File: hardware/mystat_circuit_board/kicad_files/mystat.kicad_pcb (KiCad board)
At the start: 4 copper layers, 60 x 81 mm, 93 parts, among them J1 PJ-063AH, J2 2173157-3, J3 SJ1-42534-SMT, K1 9011-05-11, K2 9011-05-11, K3 9011-05-11, K4 9011-05-11, K5 9011-05-11, P1 ICSP, U10 OPA192, U11 BUF634A, U12 ADG1419, U13 OPA192, U14 OPA192, U15 OPA192, U16 OPA192, U17 OPA192, U2 LTM8045, U3 ADP7182AUJZ-R7, U4 ADP7118AUJZ-5.0-R7, U5 PIC16F1459, U6 ADR421, U7 MCP3550-60, U8 MCP3550-60, U9 DAC1220, X1 2.5 MHz

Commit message: schematic: change electrode connections to screw terminals, BUF634A to HSOIC version with thermal pad
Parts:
- C10, C11, C12, C13, C14, C15, C17, C18, C2, C23, C25, C26, C27, C28, C29, C30, C31, C32, C34, C35, C36, C37: value 0.1 µF -> 100 nF
- C16: value 10 µF -> 10 uF
- C3: value 47 μF -> 47 uF
- C39, C5, C6, C8, C9: value 4.7 µF -> 4.7 uF
- C4, C7: value 4.7 μF -> 4.7 uF
- FB1: value Ferrite_Bead -> 32 Ω
- U11: value BUF634A -> BUF634AIDDAR; footprint my_footprints:SOIC-8 -> Package_SO:TI_SO-PowerPAD-8_ThermalVias
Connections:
- J2 pad 4: (no net) -> unconnected-(J2-Pad4)
- P1 pad 6: (no net) -> unconnected-(P1-Pin_6-Pad6)
- U11 pad 1: (no net) -> unconnected-(U11-BW-Pad1)
- U11 pad 2: (no net) -> unconnected-(U11-NC-Pad2)
- U11 pad 5: (no net) -> unconnected-(U11-NC-Pad5)
- U11 pad 8: (no net) -> unconnected-(U11-NC-Pad8)
- U12 pad 5: (no net) -> unconnected-(U12-NC-Pad5)
- U2 pad E1: (no net) -> unconnected-(U2-PIN_E1-PadE1)
- U2 pad F1: (no net) -> unconnected-(U2-PIN_F1-PadF1)
- U5 pad 14: (no net) -> unconnected-(U5-RC2-Pad14)
- U6 pad 1: (no net) -> unconnected-(U6-TP-Pad1)
- U6 pad 3: (no net) -> unconnected-(U6-NIC-Pad3)
- U6 pad 5: (no net) -> unconnected-(U6-TRIM-Pad5)
- U6 pad 7: (no net) -> unconnected-(U6-NIC-Pad7)
- U6 pad 8: (no net) -> unconnected-(U6-TP-Pad8)
- U9 pad 6: (no net) -> unconnected-(U9-DNC-Pad6)
- U9 pad 7: (no net) -> unconnected-(U9-DNC-Pad7)
- U9 pad 8: (no net) -> unconnected-(U9-DNC-Pad8)
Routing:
- net Net-(U10-~): track 11.5 -> 0.00 mm
- net (no net): track 0.00 -> 11.5 mm
- net GND: vias 55 -> 54
- added copper zone on B.Cu, net -13.4V

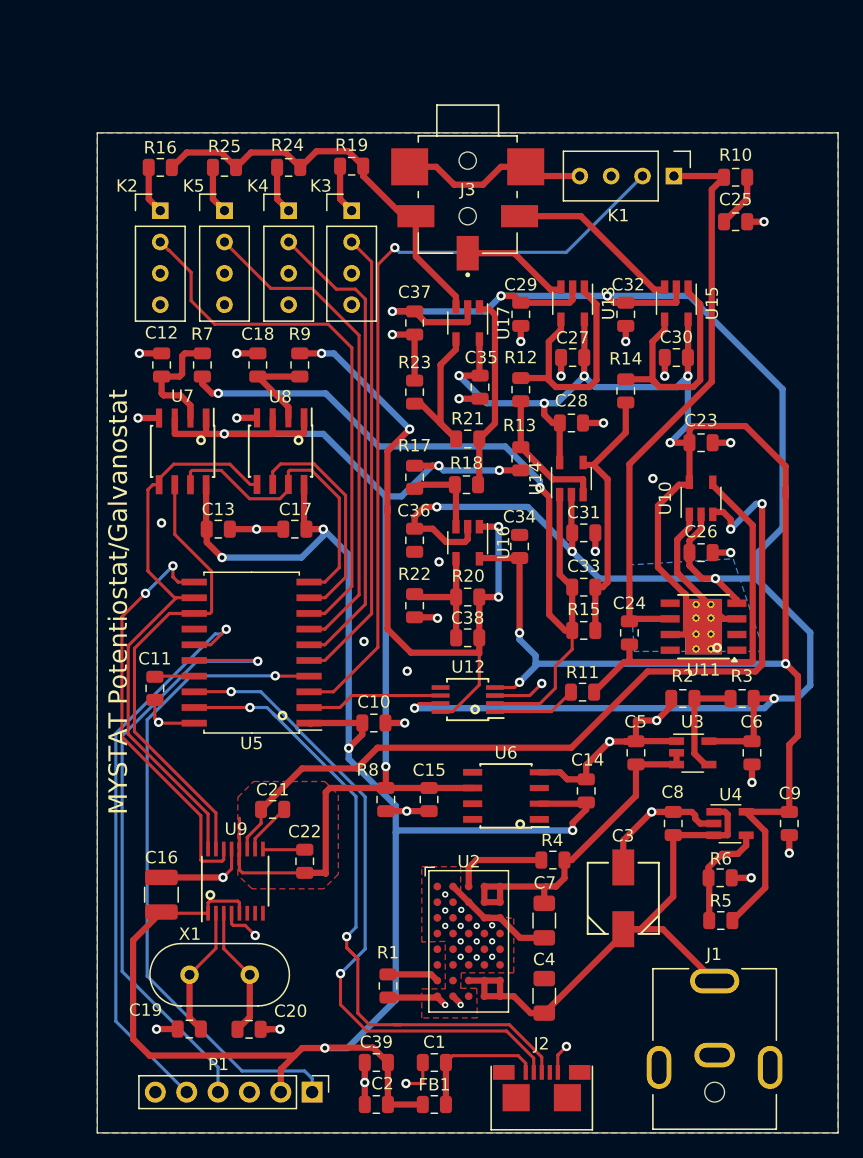
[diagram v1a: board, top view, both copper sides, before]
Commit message: change micro USB to USB C 16P 2.0, rotate U11 for routing of thermal pad version
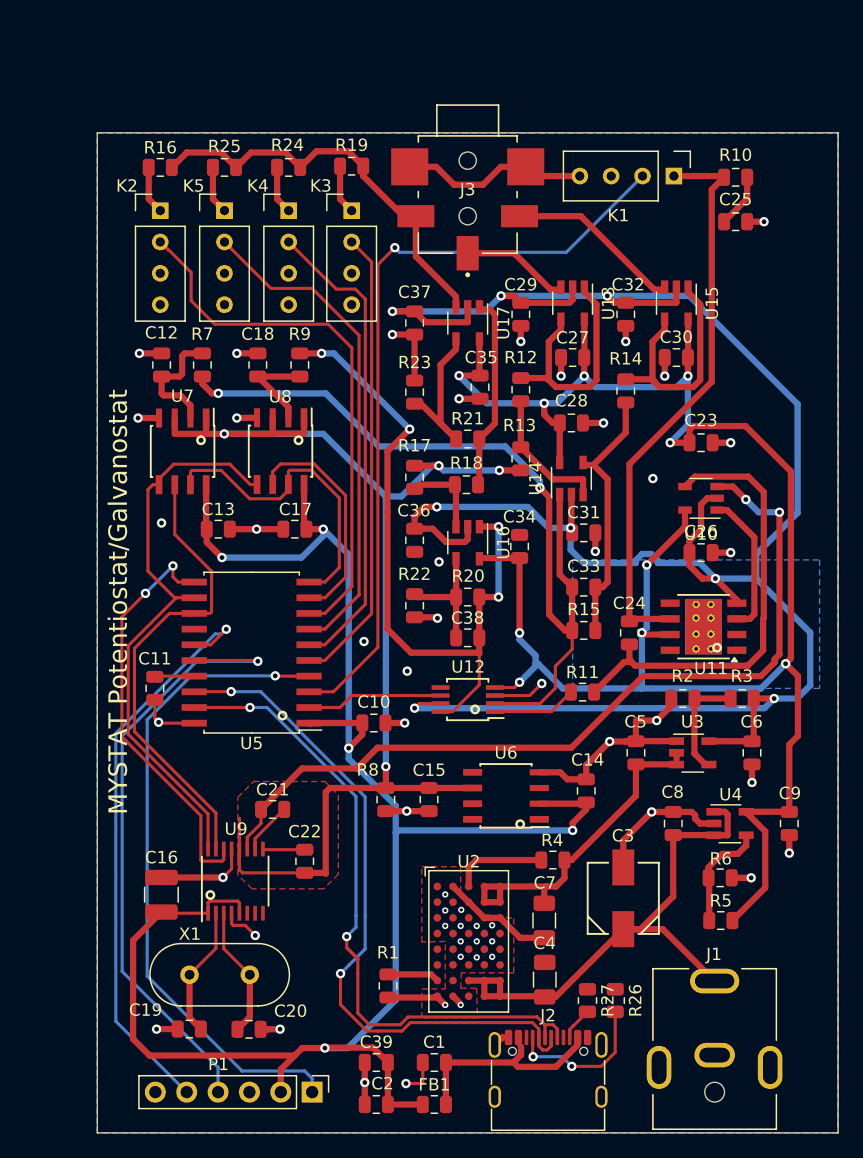
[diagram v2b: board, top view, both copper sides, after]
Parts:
- added R26: 5.1k, Resistor_SMD:R_0805_2012Metric, F.Cu at (92.0, 120.3)
- added R27: 5.1k, Resistor_SMD:R_0805_2012Metric, F.Cu at (89.7, 120.3)
- J2: value 2173157-3 -> ~; footprint my_footprints:CONN_2173157-3 -> my_footprints:USB_C_Receptacle_G-Switch_GT-USB-7010ASV
- U7, U8: value MCP3550-60 -> MCP3551
- moved C4 1.31 mm to (86.2, 118.6)
- moved J2 1.03 mm to (86.5, 127.0)
- turned U10 to 180 degrees
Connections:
- J2 pad 1: Net-(C1-Pad2) -> GND
- J2 pad 2: Net-(U5-D-) -> GND
- J2 pad 3: Net-(U5-D+) -> GND
- J2 pad 4: unconnected-(J2-Pad4) -> GND
- U5 pad 18: Net-(U5-D-) -> /digital/D-
- U5 pad 19: Net-(U5-D+) -> /digital/D+
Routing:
- net /digital/D-: track 0.00 -> 55.4 mm, vias 0 -> 2
- net /digital/D+: track 0.00 -> 54.4 mm, vias 0 -> 2
- net Net-(U5-D+): track 54.0 -> 0.00 mm, vias 2 -> 0
- net Net-(U5-D-): track 53.2 -> 0.00 mm, vias 2 -> 0
- net Net-(J2-CC1): track 0.00 -> 12.3 mm, vias 0 -> 2
- net Net-(U10-~): track 0.00 -> 11.7 mm
- net (no net): track 11.5 -> 0.00 mm
- net Net-(C1-Pad2): track 11.1 -> 19.2 mm
- net GND: track 635.0 -> 641.2 mm, vias 54 -> 53
- net Net-(U10--): track 31.2 -> 36.9 mm
- net -13.4V: track 179.2 -> 184.8 mm
- net Net-(J2-CC2): track 0.00 -> 2.68 mm
- net +15V: track 46.5 -> 45.2 mm
- net +13.4V: track 159.4 -> 159.6 mm, vias 8 -> 10
- added copper zone on In1.Cu, net -13.4V
- added copper zone on In2.Cu, net -13.4V

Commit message: partway through adding normal reed relay size
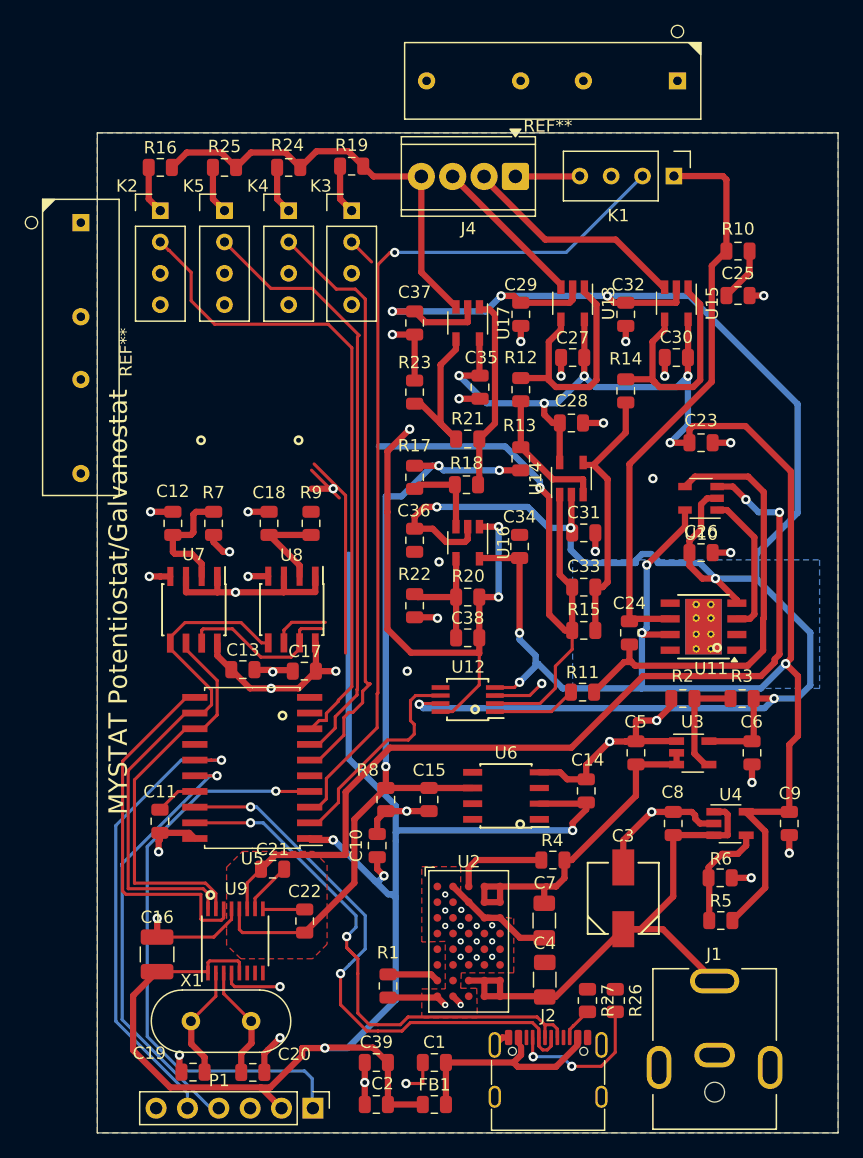
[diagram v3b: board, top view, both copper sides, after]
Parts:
- removed J3: SJ1-42534-SMT, my_footprints:CUI_SJ1-42534-SMT
- added J4: Screw_Terminal_01x04, TerminalBlock_Phoenix:TerminalBlock_Phoenix_MPT-0,5-4-2.54_1x04_P2.54mm_Horizontal, F.Cu at (83.9, 53.5)
- added REF**: Reed_Relay_MiRelay_SIP-HV1A05D, my_footprints:Reed_Relay_MiRelay_SIP-HV1A05D, F.Cu at (48.7, 57.3)
- added REF**: Reed_Relay_MiRelay_SIP-HV1A05D, my_footprints:Reed_Relay_MiRelay_SIP-HV1A05D, F.Cu at (97.0, 45.8)
- moved C12 12.9 mm to (56.1, 81.6)
- moved C18 12.9 mm to (63.9, 81.6)
- moved R7 12.9 mm to (59.4, 81.6)
- moved R9 12.9 mm to (67.3, 81.6)
- moved U7 12.9 mm to (57.8, 88.6)
- moved U8 12.9 mm to (65.7, 88.6)
- moved C13 11.6 mm to (61.8, 93.5)
- moved C17 11.5 mm to (66.8, 93.6)
- moved C11 10.8 mm to (55.1, 105.8)
- moved C10 9.93 mm to (72.7, 107.7), turned to 90 degrees
- moved U5 9.34 mm to (62.5, 101.4)
- moved C25 5.98 mm to (101.9, 63.2)
- moved R10 5.98 mm to (101.9, 59.6)
- moved C16 4.84 mm to (54.8, 116.5)
- moved C21 4.84 mm to (64.2, 109.6)
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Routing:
- net RANGE3: track 37.4 -> 2.29 mm
- net Vref: track 98.4 -> 82.2 mm
- net V_MEAS: track 67.0 -> 52.2 mm
- net Net-(P1-Pin_4): track 50.8 -> 36.1 mm
- net SDIO2: track 18.5 -> 4.65 mm
- net GND: track 641.2 -> 629.1 mm, vias 53 -> 50
- net CS2: track 25.4 -> 13.7 mm
- net WE: track 15.3 -> 5.23 mm
- net I_MEAS: track 56.8 -> 66.7 mm
- net RANGE2: track 38.7 -> 48.4 mm
- net /digital/D-: track 55.4 -> 45.8 mm
- net /digital/D+: track 54.4 -> 44.8 mm
- net RANGE1: track 40.2 -> 49.3 mm
- net RANGE4: track 44.1 -> 53.1 mm
- net Net-(P1-Pin_5): track 47.0 -> 38.2 mm
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
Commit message: progress save with layout
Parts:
- removed REF** (x2): Reed_Relay_MiRelay_SIP-HV1A05D, my_footprints:Reed_Relay_MiRelay_SIP-HV1A05D
- removed REF**: LOGO, my_footprints:GPLv3_2
- removed REF**: OSHW-Logo2_14.6x12mm_SilkScreen, Symbol:OSHW-Logo2_14.6x12mm_SilkScreen
- K1, K2, K3, K4, K5: value 9011-05-11 -> ~; footprint my_footprints:relay_9011-05-11 -> my_footprints:Reed_Relay_MiRelay_SIP-HV1A05D
- moved K3 21.6 mm to (77.3, 76.8), turned to 90 degrees
- moved K4 21.1 mm to (70.3, 76.8), turned to 90 degrees
- moved K5 20.7 mm to (63.2, 76.8), turned to 90 degrees
- moved K2 20.6 mm to (56.1, 76.8), turned to 90 degrees
- moved R10 13.6 mm to (99.3, 73.0), turned to -90 degrees
- moved C25 11.7 mm to (96.8, 73.7), turned to 90 degrees
- moved C37 11.6 mm to (81.9, 55.6), turned to 90 degrees
- moved J4 11.4 mm to (95.2, 53.8)
- moved R23 10.3 mm to (82.9, 63.7), turned to 180 degrees
- moved K1 7.41 mm to (104.1, 53.3)
- moved R19 7.32 mm to (77.9, 52.7)
- moved U17 6.97 mm to (83.7, 59.5)
- moved R21 5.96 mm to (85.2, 71.9)
- moved C23 5.66 mm to (104.1, 77.4)
- moved C28 5.52 mm to (92.5, 69.8)
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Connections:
- K1 pad 1: Net-(C24-Pad1) -> WE
- K1 pad 2: CELL_ON -> GND
- K1 pad 3: GND -> CELL_ON
- K1 pad 4: WE -> Net-(C24-Pad1)
- K2 pad 1: Net-(K2-~-Pad1) -> GND
- K2 pad 2: RANGE4 -> GND
- K2 pad 3: GND -> RANGE4
- K2 pad 4: GND -> Net-(K2-Pad4)
- K3 pad 1: Net-(K3-~-Pad1) -> GND
- K3 pad 2: RANGE3 -> GND
- K3 pad 3: GND -> RANGE3
- K3 pad 4: GND -> Net-(K3-Pad4)
- K4 pad 1: Net-(K4-~-Pad1) -> GND
- K4 pad 2: RANGE2 -> GND
- K4 pad 3: GND -> RANGE2
- K4 pad 4: GND -> Net-(K4-Pad4)
- K5 pad 1: Net-(K5-~-Pad1) -> GND
- K5 pad 2: RANGE1 -> GND
- K5 pad 3: GND -> RANGE1
- K5 pad 4: GND -> Net-(K5-Pad4)
- R16 pad 2: Net-(K2-~-Pad1) -> Net-(K2-Pad4)
- R19 pad 2: Net-(K3-~-Pad1) -> Net-(K3-Pad4)
- R24 pad 2: Net-(K4-~-Pad1) -> Net-(K4-Pad4)
- R25 pad 2: Net-(K5-~-Pad1) -> Net-(K5-Pad4)
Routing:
- net RANGE3: track 2.29 -> 41.7 mm
- net GND: track 629.1 -> 653.1 mm, vias 50 -> 55
- net I_MEAS: track 66.7 -> 44.4 mm
- net Net-(C24-Pad1): track 46.8 -> 29.7 mm
- net Net-(U10--): track 36.9 -> 21.7 mm, vias 0 -> 2
- net V_MEAS: track 52.2 -> 67.2 mm
- net Vref: track 82.2 -> 96.1 mm
- net RE: track 18.4 -> 5.97 mm
- net +5V: track 140.7 -> 128.3 mm, vias 6 -> 5
- net Net-(U17-~): track 15.8 -> 26.0 mm
- net Net-(U15--): track 20.0 -> 29.7 mm
- net SDIO2: track 4.65 -> 12.8 mm
- net RANGE2: track 48.4 -> 40.3 mm
- net CS2: track 13.7 -> 21.0 mm
- net RANGE1: track 49.3 -> 42.2 mm
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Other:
- board text added: "Eclectic version 8"
- board text removed: "Lucky version 7"

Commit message: more pcb layout progress save
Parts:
- C3: footprint my_footprints:EEE-FT1V470AR -> easyeda2kicad:CAP-SMD_BD5.0-L5.3-W5.3-LS6.0-FD
- FB1: value 32 Ω -> 33 Ω
- J4: footprint TerminalBlock_Phoenix:TerminalBlock_Phoenix_MPT-0,5-4-2.54_1x04_P2.54mm_Horizontal -> easyeda2kicad:CONN-TH_4P-P2.54_MX128-2.54-GN01-04P-CU-Y-A
- moved J4 4.08 mm to (91.2, 53.8)
- moved C4 3.78 mm to (86.3, 114.8)
- moved C7 3.78 mm to (86.2, 110.0)
- moved U2 3.78 mm to (80.1, 111.7)
- moved R1 3.78 mm to (73.6, 115.3)
- moved C14 3.37 mm to (89.5, 99.9)
- moved U6 3.09 mm to (84.3, 100.8)
- moved R4 2.96 mm to (87.0, 105.9)
- moved C15 2.81 mm to (78.9, 101.2)
- moved R11 2.61 mm to (90.2, 92.9)
- moved R8 1.81 mm to (76.4, 102.7)
- moved R27 1.41 mm to (88.3, 120.1)
- moved R26 0.88 mm to (91.1, 120.1)
- moved C37 0.53 mm to (82.1, 55.1)
- moved C23 0.30 mm to (104.0, 77.1)
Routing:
- net GND: track 653.1 -> 619.4 mm, vias 55 -> 56
- net Net-(C1-Pad2): track 18.2 -> 28.0 mm, vias 0 -> 2
- net /digital/D-: track 49.0 -> 45.9 mm
- net Net-(U12-D): track 6.81 -> 9.41 mm
- net Net-(U10--): track 21.7 -> 19.4 mm
- net /digital/D+: track 48.1 -> 45.8 mm
- net Net-(C24-Pad1): track 29.7 -> 31.9 mm
- net -15V: track 28.2 -> 26.0 mm
- net Vref: track 96.1 -> 98.1 mm
- net +15V: track 45.1 -> 43.5 mm
- net -13.4V: track 185.2 -> 186.8 mm
- net DAC_out: track 72.9 -> 74.4 mm
- net Net-(J2-CC1): track 12.3 -> 13.7 mm, vias 2 -> 0
- net Net-(U2-PIN_A3): track 7.66 -> 6.86 mm
- net +5V: track 128.3 -> 129.1 mm
- added copper zone on F.Cu, net -13.4V

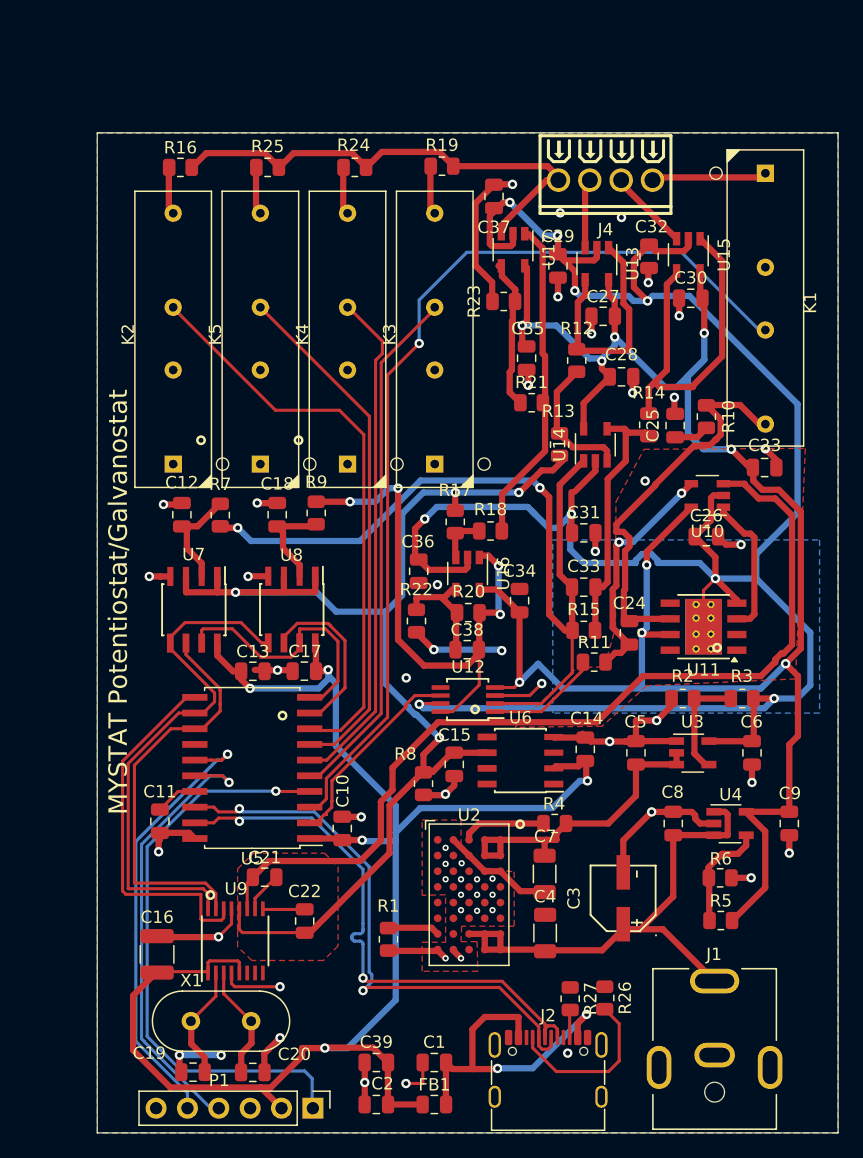
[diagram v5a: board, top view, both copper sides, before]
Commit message: silkscreen changes
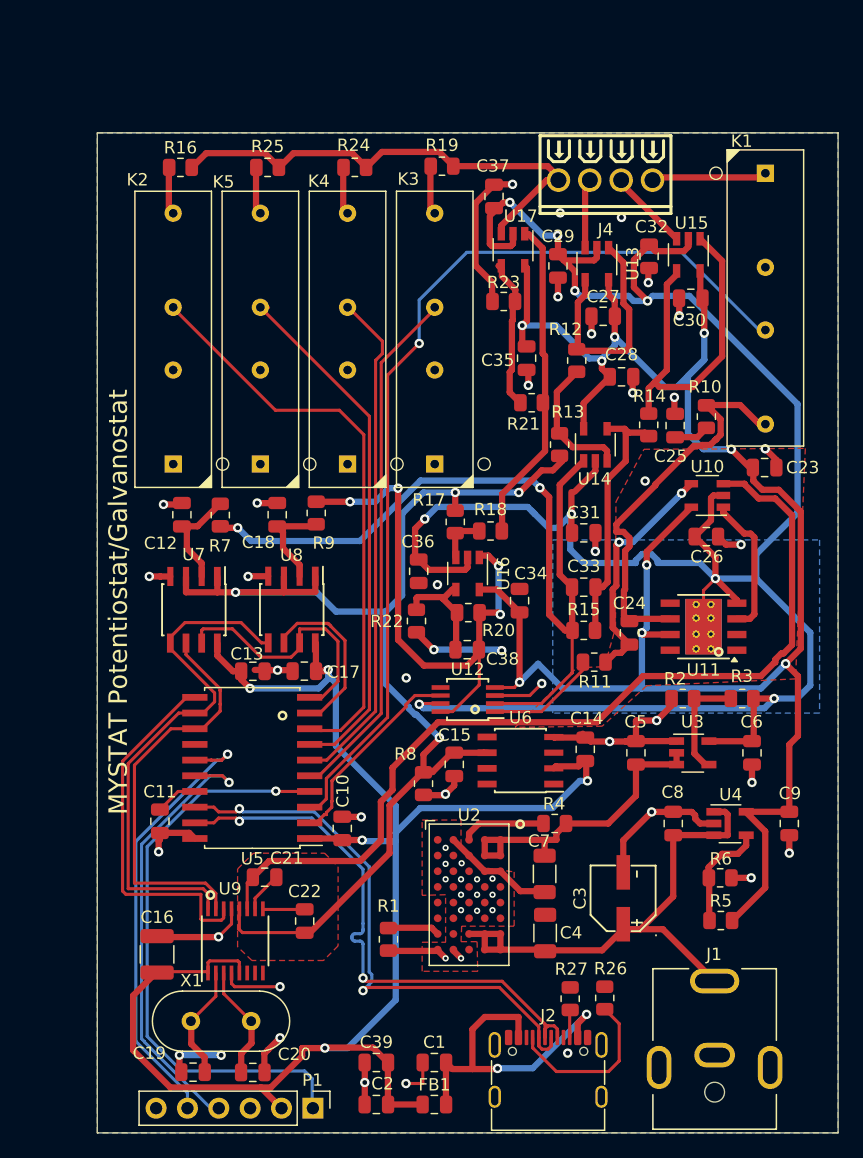
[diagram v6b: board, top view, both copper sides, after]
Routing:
- net GND: track 619.4 -> 617.8 mm
